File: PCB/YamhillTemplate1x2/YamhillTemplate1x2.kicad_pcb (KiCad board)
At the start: 2 copper layers, 6 parts

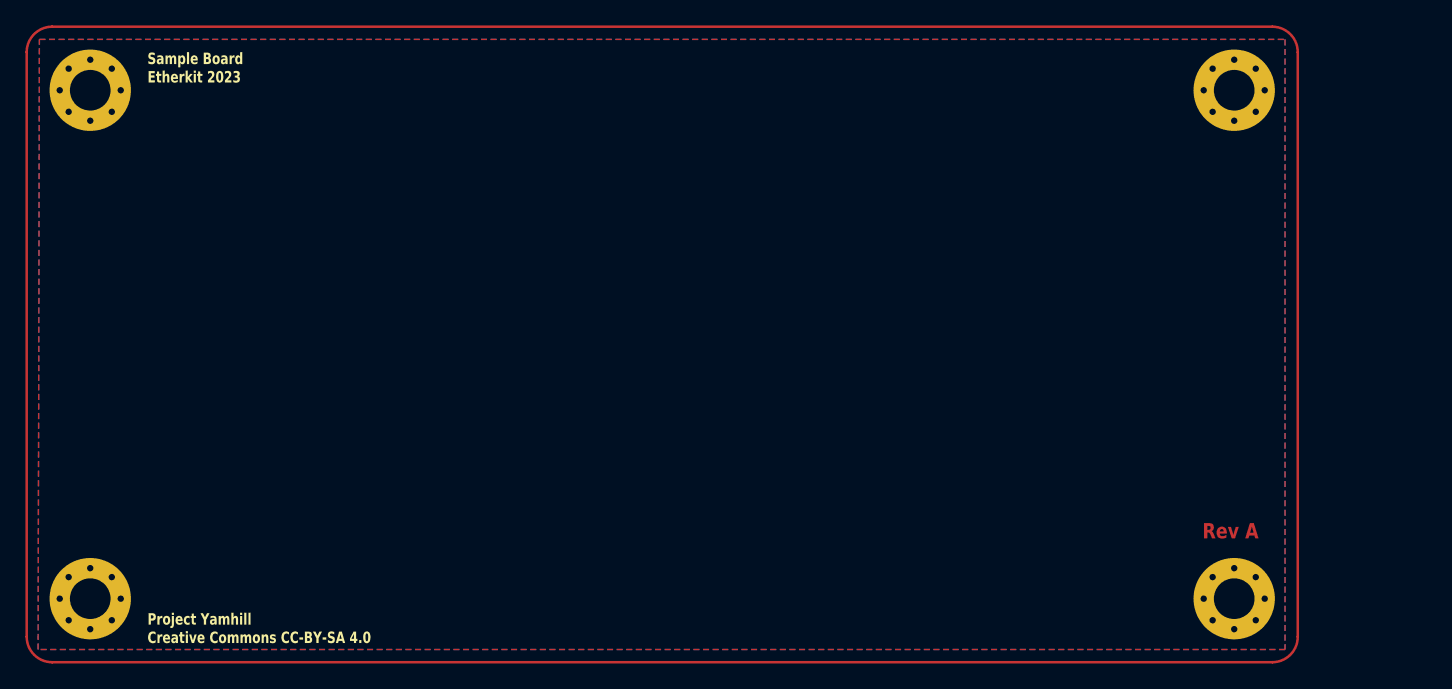
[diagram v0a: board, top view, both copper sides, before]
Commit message: Fix PCB template problems
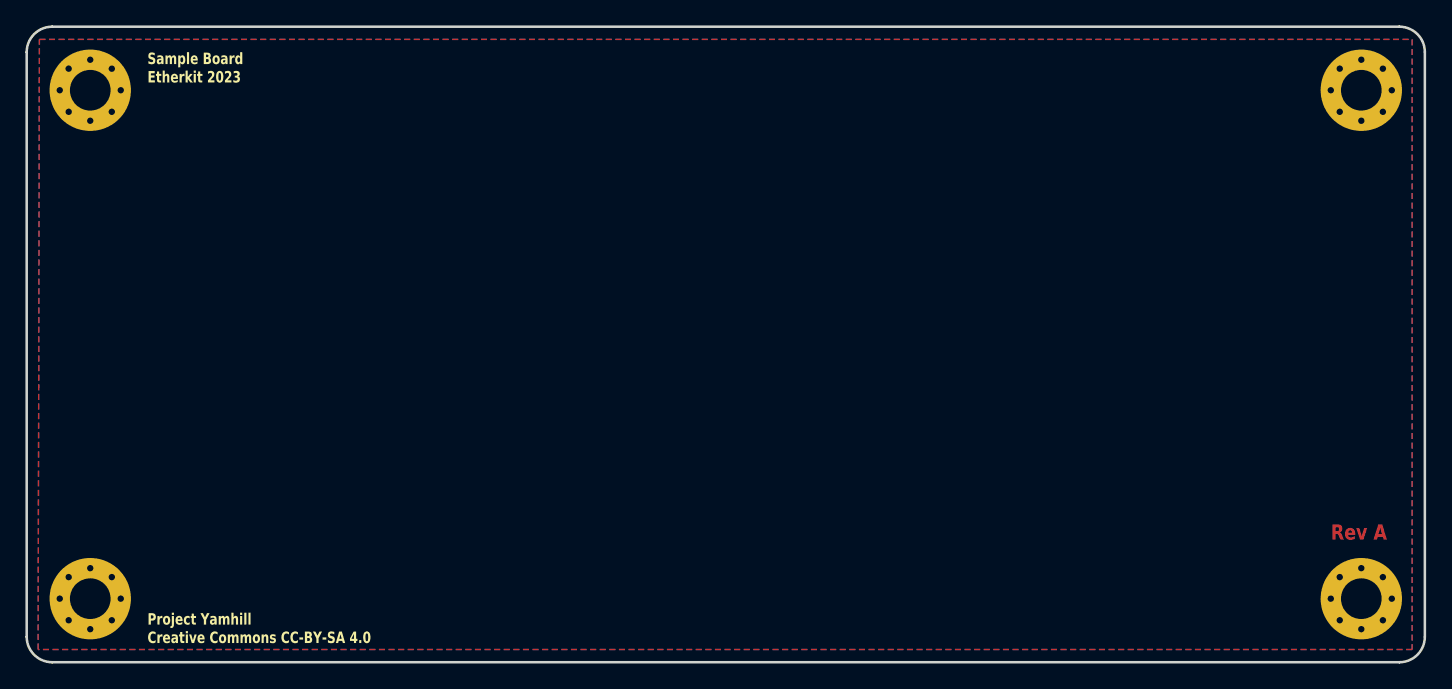
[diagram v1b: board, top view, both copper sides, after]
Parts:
- removed REF** (x4): MountingHole_3.2mm_M3_Pad_Via, MountingHole:MountingHole_3.2mm_M3_Pad_Via
- added H1: MountingHole_Pad, MountingHole:MountingHole_3.2mm_M3_Pad_Via, F.Cu at (105.0, 55.0)
- added H2: MountingHole_Pad, MountingHole:MountingHole_3.2mm_M3_Pad_Via, F.Cu at (205.0, 55.0)
- added H3: MountingHole_Pad, MountingHole:MountingHole_3.2mm_M3_Pad_Via, F.Cu at (105.0, 95.0)
- added H4: MountingHole_Pad, MountingHole:MountingHole_3.2mm_M3_Pad_Via, F.Cu at (205.0, 95.0)
- moved Ref** 10.0 mm to (204.9, 88.1)
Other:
- board outline added: 110 x 50 mm
